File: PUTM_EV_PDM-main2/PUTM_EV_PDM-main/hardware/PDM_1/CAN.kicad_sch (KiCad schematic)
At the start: 9 parts, among them U5 MCP2542FDxMF

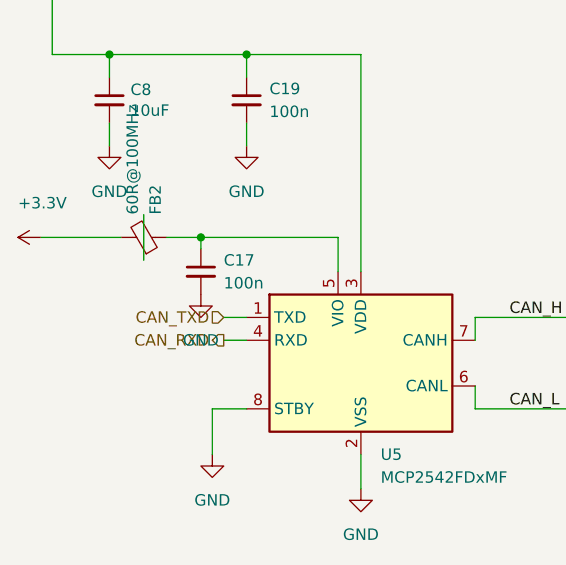
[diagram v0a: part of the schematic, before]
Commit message: lepsze footprinty
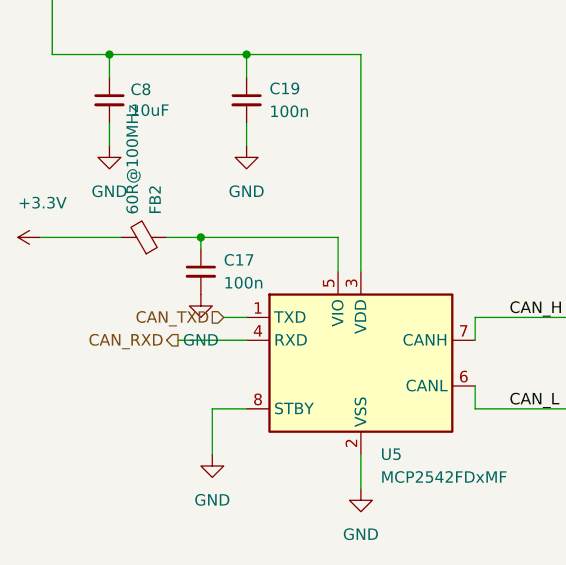
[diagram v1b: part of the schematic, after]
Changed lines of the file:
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@@
-    (stroke (width 0) (type default))
-  )
-  (wire (pts (xy 105.41 85.09) (xy 105.41 80.01))
     (stroke (width 0) (type default))
   )
@@
     (stroke (width 0) (type default))
   )
-  (wire (pts (xy 114.3 93.98) (xy 116.84 93.98))
+  (wire (pts (xy 109.22 93.98) (xy 116.84 93.98))
     (stroke (width 0) (type default))
   )
@@
     (effects (font (size 1.27 1.27)) (justify left))
   )
-  (hierarchical_label "CAN_RXD" (shape output) (at 114.3 93.98 180) (fields_autoplaced)
+  (hierarchical_label "CAN_RXD" (shape output) (at 109.22 93.98 180) (fields_autoplaced)
     (effects (font (size 1.27 1.27)) (justify right))
   )

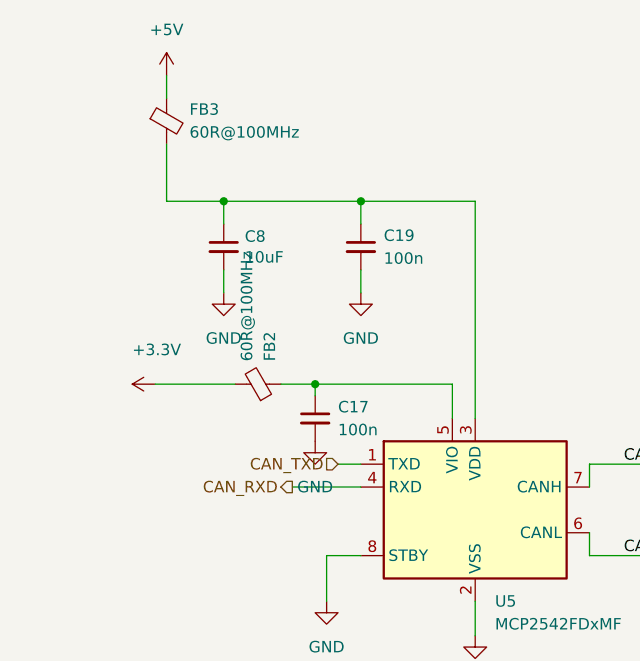
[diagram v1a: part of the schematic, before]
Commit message: nowe połączenia
dodane połączenia z STM
dodane złącza
dodane LED
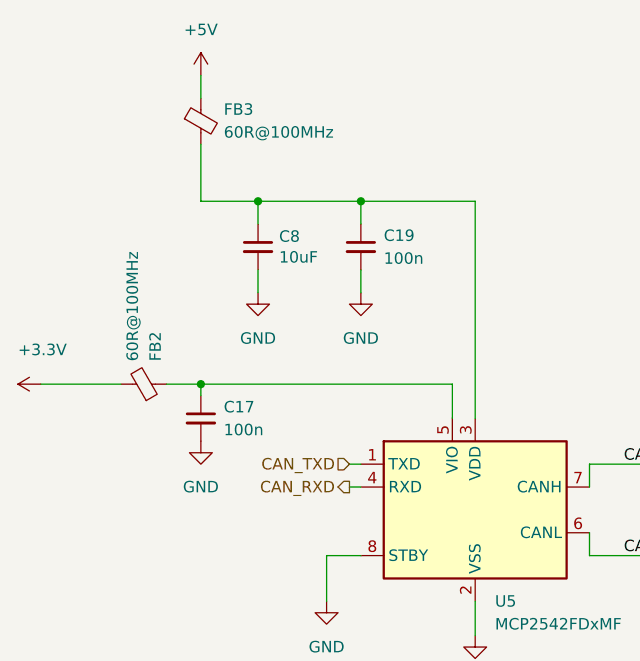
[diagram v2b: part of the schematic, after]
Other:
- moved on the sheet: C17, C8, FB2, FB3

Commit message: Koniec połączeń sygnałów
Wszystkie sygnały z stm poprowadzone
Zmienione ułożenie połączeń do złącz
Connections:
- net CAN_VDD: now reaches C19.1, C8.1, FB3.2, U5.3 (VDD)
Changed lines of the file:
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@@
   (junction (at 191.77 85.09) (diameter 0) (color 0 0 0 0)
   )
+  (junction (at 124.46 62.23) (diameter 0) (color 0 0 0 0)
+  )
+  (junction (at 124.46 82.55) (diameter 0) (color 0 0 0 0)
+  )
   (junction (at 116.84 62.23) (diameter 0) (color 0 0 0 0)
   )
@@
     (stroke (width 0) (type default))
   )
-  (wire (pts (xy 99.06 82.55) (xy 127 82.55))
+  (wire (pts (xy 99.06 82.55) (xy 124.46 82.55))
     (stroke (width 0) (type default))
   )
@@
     (stroke (width 0) (type default))
   )
-  (wire (pts (xy 116.84 62.23) (xy 129.54 62.23))
+  (wire (pts (xy 116.84 62.23) (xy 124.46 62.23))
     (stroke (width 0) (type default))
   )
@@
     (stroke (width 0) (type default))
   )
+  (wire (pts (xy 124.46 62.23) (xy 129.54 62.23))
+    (stroke (width 0) (type default))
+  )
   (wire (pts (xy 142.24 101.6) (xy 154.94 101.6))
+    (stroke (width 0) (type default))
+  )
+  (wire (pts (xy 124.46 82.55) (xy 127 82.55))
     (stroke (width 0) (type default))
   )
@@
   (label "CAN_H" (at 146.05 91.44 0) (fields_autoplaced)
     (effects (font (size 1.27 1.27)) (justify left bottom))
+  )
+  (label "CAN_VDD" (at 100.33 62.23 0) (fields_autoplaced)
+    (effects (font (size 0.5 0.5)) (justify left bottom))
   )
   (hierarchical_label "CAN_H" (shape bidirectional) (at 154.94 91.44 0) (fields_autoplaced)
@@
     )
   )
+  (symbol (lib_id "power:PWR_FLAG") (at 124.46 82.55 0) (unit 1)
+    (in_bom yes) (on_board yes) (dnp no) (fields_autoplaced)
+    (property "Reference" "#FLG02" (at 124.46 80.645 0)
+      (effects (font (size 1.27 1.27)) hide)
+    )
+    (property "Value" "PWR_FLAG" (at 124.46 77.47 0)
+      (effects (font (size 1.27 1.27)))
+    )
+    (property "Footprint" "" (at 124.46 82.55 0)
+      (effects (font (size 1.27 1.27)) hide)
+    )
+    (property "Datasheet" "~" (at 124.46 82.55 0)
+      (effects (font (size 1.27 1.27)) hide)
+    )
+    (pin "1")
+    (instances
+      (project "PDM_1"
+        (path "/b652b05a-4e3d-4ad1-b032-18886abe7d45/ae0773d9-e23d-47b1-916b-0288055270db"
+          (reference "#FLG02") (unit 1)
+        )
+      )
+    )
+  )
   (symbol (lib_id "Device:FerriteBead_Small") (at 99.06 53.34 0) (unit 1)
     (in_bom yes) (on_board yes) (dnp no) (fields_autoplaced)
@@
         )
       )
+    )
+  )
+  (symbol (lib_id "power:PWR_FLAG") (at 124.46 62.23 0) (unit 1)
+    (in_bom yes) (on_board yes) (dnp no) (fields_autoplaced)
+    (property "Reference" "#FLG07" (at 124.46 60.325 0)
+      (effects (font (size 1.27 1.27)) hide)
+    )
+    (property "Value" "PWR_FLAG" (at 124.46 57.15 0)
+      (effects (font (size 1.27 1.27)))
+    )
+    (property "Footprint" "" (at 124.46 62.23 0)
+      (effects (font (size 1.27 1.27)) hide)
+    )
+    (property "Datasheet" "~" (at 124.46 62.23 0)
+      (effects (font (size 1.27 1.27)) hide)
+    )
+    (pin "1")
+    (instances
+      (project "PDM_1"
+        (path "/b652b05a-4e3d-4ad1-b032-18886abe7d45/ae0773d9-e23d-47b1-916b-0288055270db"
+          (reference "#FLG07") (unit 1)
+        )
+      )
